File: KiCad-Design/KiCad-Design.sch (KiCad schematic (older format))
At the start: 66 parts, among them J1 USB_B_Micro, J2 Battery, J3 Ext, J4 OLED, Q1 SI2301, Q2 SI2301, Q3 SI2307CDS-T1-GE3, SW1 MCU BLE Adv, SW2 MCU FLASH, SW3 MCU RESET, U1 PMBT3904, U2 BME280, U3 CP2104, U4 LTC4054ES5-4.2, U5 PMBT3904, U6 PMBT3904, U7 BME680, U8 AP2112K-3.3, U9 ttgo-32-micro-symbols

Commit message: PCB : Small update on the PCB design
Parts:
- added R21, R22: 4.7K, Resistor_SMD:R_0805_2012Metric, symbol Device:R
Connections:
- net +3V3: now also R21.2, R22.2
- net MCU_SCL: now also R22.1
- net MCU_SDA: now also R21.1
- no-connect marks 36 -> 37
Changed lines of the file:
@@
 encoding utf-8
 Sheet 1 1
-Title ""
-Date ""
-Rev ""
-Comp ""
+Title "Google Home Environment Node"
+Date "2021-03-01"
+Rev "v1"
+Comp "RS System"
 Comment1 ""
 Comment2 ""
@@
 P 3000 5550
 F 0 "C6" V 3050 5450 50  0000 C CNN
-F 1 "100pF" V 3050 5700 50  0000 C CNN
+F 1 "100pF" V 3050 5700 50  0001 C CNN
 F 2 "Capacitor_SMD:C_0805_2012Metric" H 3038 5400 50  0001 C CNN
 F 3 "~" H 3000 5550 50  0001 C CNN
@@
 Wire Wire Line
 	5850 1900 5550 1900
-Text GLabel 5750 1300 2    50   BiDi Italic 0
+Text GLabel 5900 1300 2    50   BiDi Italic 0
 Sensor_add
-Wire Wire Line
-	5550 1300 5750 1300
-Text GLabel 5750 1700 2    50   BiDi Italic 0
+Text GLabel 5900 1700 2    50   BiDi Italic 0
 MCU_SDA
-Text GLabel 5750 1500 2    50   BiDi Italic 0
+Text GLabel 5900 1500 2    50   BiDi Italic 0
 MCU_SCL
-Wire Wire Line
-	5550 1500 5750 1500
-Wire Wire Line
-	5750 1700 5550 1700
 Wire Wire Line
 	4850 2200 4850 2300
@@
 	5200 5900 5150 5900
 Connection ~ 5150 5900
+NoConn ~ 5300 3950
+Wire Wire Line
+	5550 1300 5900 1300
+Wire Wire Line
+	5550 1500 5800 1500
+Wire Wire Line
+	5550 1700 5650 1700
+$Comp
+L Device:R R21
+U 1 1 60581768
+P 5650 1050
+F 0 "R21" V 5700 900 50  0000 C CNN
+F 1 "4.7K" V 5750 1050 50  0000 C CNN
+F 2 "Resistor_SMD:R_0805_2012Metric" V 5580 1050 50  0001 C CNN
+F 3 "~" H 5650 1050 50  0001 C CNN
+	1    5650 1050
+	-1   0    0    1
+$EndComp
+$Comp
+L Device:R R22
+U 1 1 605821B2
+P 5800 1050
+F 0 "R22" V 5850 900 50  0000 C CNN
+F 1 "4.7K" V 5700 1050 50  0000 C CNN
+F 2 "Resistor_SMD:R_0805_2012Metric" V 5730 1050 50  0001 C CNN
+F 3 "~" H 5800 1050 50  0001 C CNN
+	1    5800 1050
+	-1   0    0    1
+$EndComp
+$Comp
+L power:+3.3V #PWR051
+U 1 1 60582A40
+P 5900 650
+F 0 "#PWR051" H 5900 500 50  0001 C CNN
+F 1 "+3.3V" V 5915 778 50  0000 L CNN
+F 2 "" H 5900 650 50  0001 C CNN
+F 3 "" H 5900 650 50  0001 C CNN
+	1    5900 650
+	0    1    1    0
+$EndComp
+Wire Wire Line
+	5800 1200 5800 1500
+Connection ~ 5800 1500
+Wire Wire Line
+	5800 1500 5900 1500
+Wire Wire Line
+	5650 1200 5650 1700
+Connection ~ 5650 1700
+Wire Wire Line
+	5650 1700 5900 1700
+Wire Wire Line
+	5650 900  5650 650
+Wire Wire Line
+	5650 650  5800 650
+Wire Wire Line
+	5800 900  5800 650
+Connection ~ 5800 650
+Wire Wire Line
+	5800 650  5900 650
 $EndSCHEMATC

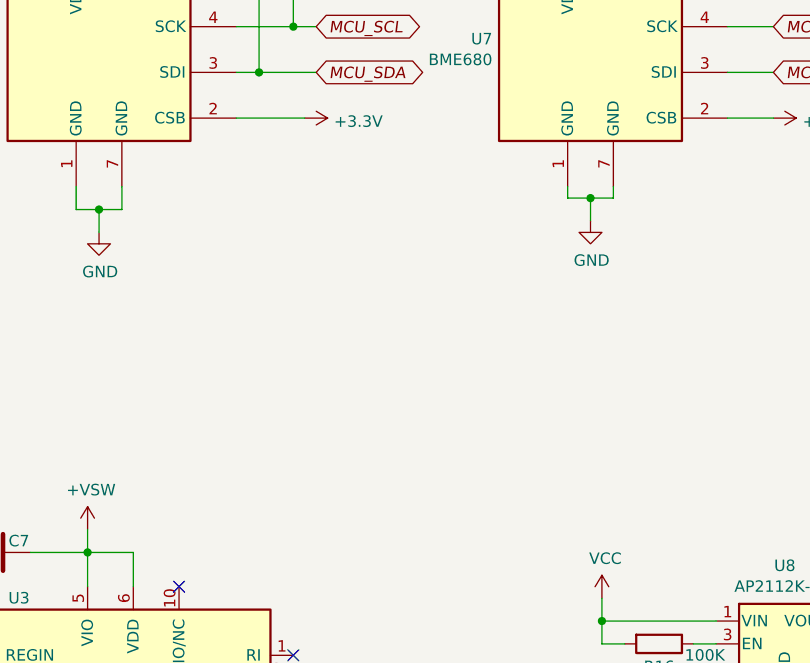
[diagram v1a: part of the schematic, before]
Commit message: PCB : Adding HDC1080 in the design
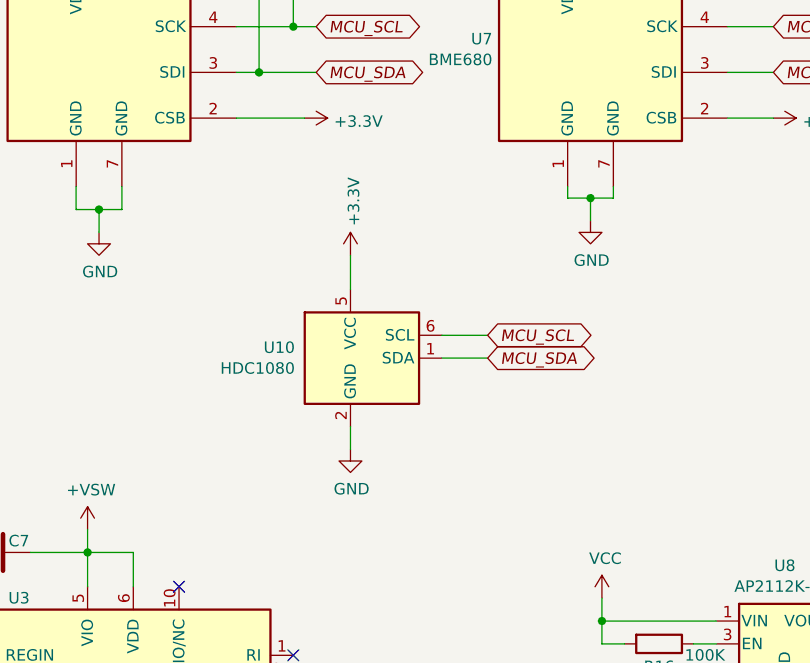
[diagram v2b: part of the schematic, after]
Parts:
- added U10: HDC1080, Package_SON:Texas_PWSON-N6, symbol Sensor_Humidity:HDC1080
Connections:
- net +3V3: now also U10.5 (VCC)
- net GND: now also U10.2 (GND)
- net MCU_SCL: now also U10.6 (SCL)
- net MCU_SDA: now also U10.1 (SDA)
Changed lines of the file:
@@
 Wire Wire Line
 	5800 650  5900 650
+$Comp
+L Sensor_Humidity:HDC1080 U10
+U 1 1 60508683
+P 6150 2950
+F 0 "U10" H 5807 2996 50  0000 R CNN
+F 1 "HDC1080" H 5807 2905 50  0000 R CNN
+F 2 "Package_SON:Texas_PWSON-N6" H 6100 2700 50  0001 L CNN
+F 3 "http://www.ti.com/lit/ds/symlink/hdc1080.pdf" H 5750 3200 50  0001 C CNN
+	1    6150 2950
+	1    0    0    -1
+$EndComp
+$Comp
+L power:+3.3V #PWR052
+U 1 1 60509223
+P 6050 2500
+F 0 "#PWR052" H 6050 2350 50  0001 C CNN
+F 1 "+3.3V" V 6065 2628 50  0000 L CNN
+F 2 "" H 6050 2500 50  0001 C CNN
+F 3 "" H 6050 2500 50  0001 C CNN
+	1    6050 2500
+	1    0    0    -1
+$EndComp
+$Comp
+L power:GND #PWR053
+U 1 1 605099FA
+P 6050 3350
+F 0 "#PWR053" H 6050 3100 50  0001 C CNN
+F 1 "GND" H 6055 3177 50  0000 C CNN
+F 2 "" H 6050 3350 50  0001 C CNN
+F 3 "" H 6050 3350 50  0001 C CNN
+	1    6050 3350
+	1    0    0    -1
+$EndComp
+Text GLabel 6650 2850 2    50   BiDi Italic 0
+MCU_SCL
+Text GLabel 6650 2950 2    50   BiDi Italic 0
+MCU_SDA
+Wire Wire Line
+	6050 2500 6050 2650
+Wire Wire Line
+	6450 2850 6650 2850
+Wire Wire Line
+	6650 2950 6450 2950
+Wire Wire Line
+	6050 3250 6050 3350
 $EndSCHEMATC

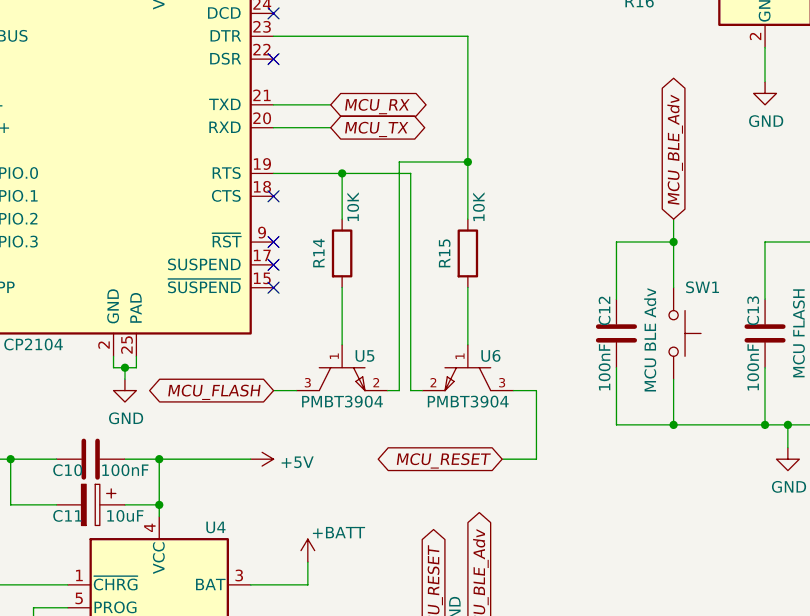
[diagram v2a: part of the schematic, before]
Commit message: PCB : Using UMH3N package instead of PMBT3904
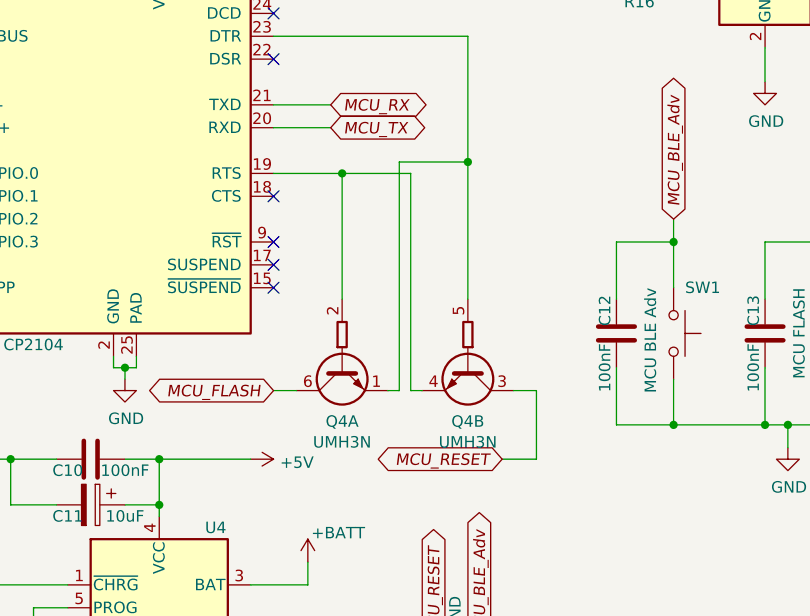
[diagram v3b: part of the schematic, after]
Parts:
- removed R14, R15: 10K, Resistor_SMD:R_0805_2012Metric, symbol Device:R
- removed U5, U6: PMBT3904, PMBT3904:NXP-PMBT3904,215-0, symbol PMBT3904:PMBT3904,215
- added Q4: UMH3N, Package_TO_SOT_SMD:SOT-363_SC-70-6, symbol Transistor_BJT:UMH3N
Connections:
- net MCU_FLASH: now also Q4.6 (C1)
- net MCU_RESET: now also Q4.3 (C2)
- net at U3.19 (RTS): now also Q4.2 (B1), Q4.4 (E2)
- net at U3.23 (DTR): now also Q4.1 (E1), Q4.5 (B2)
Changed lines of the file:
@@
 Wire Wire Line
 	5800 4850 6050 4850
-$Comp
-L Device:R R15
-U 1 1 60443C56
-P 6650 5400
-F 0 "R15" V 6550 5400 50  0000 C CNN
-F 1 "10K" V 6700 5600 50  0000 C CNN
-F 2 "Resistor_SMD:R_0805_2012Metric" V 6580 5400 50  0001 C CNN
-F 3 "~" H 6650 5400 50  0001 C CNN
-	1    6650 5400
-	1    0    0    -1
-$EndComp
-$Comp
-L Device:R R14
-U 1 1 60464BDE
-P 6100 5400
-F 0 "R14" V 6000 5400 50  0000 C CNN
-F 1 "10K" V 6150 5600 50  0000 C CNN
-F 2 "Resistor_SMD:R_0805_2012Metric" V 6030 5400 50  0001 C CNN
-F 3 "~" H 6100 5400 50  0001 C CNN
-	1    6100 5400
-	1    0    0    -1
-$EndComp
 Wire Wire Line
 	5800 5050 6100 5050
-Wire Wire Line
-	6100 5050 6100 5250
 Wire Wire Line
 	5800 4450 6650 4450
@@
 	6350 5000 6650 5000
 Connection ~ 6650 5000
-Wire Wire Line
-	6650 5000 6650 5250
 Text GLabel 5800 6000 0    50   BiDi Italic 0
 MCU_FLASH
@@
 	0    1    1    0
 $EndComp
-$Comp
-L PMBT3904:PMBT3904,215 U6
-U 1 1 604A948E
-P 6650 5700
-F 0 "U6" V 6800 5800 50  0000 C CNN
-F 1 "PMBT3904" V 7000 5700 50  0000 C CNN
-F 2 "PMBT3904:NXP-PMBT3904,215-0" H 6650 6200 50  0001 L CNN
-F 3 "https://assets.nexperia.com/documents/data-sheet/PMBT3904.pdf" H 6650 6300 50  0001 L CNN
-F 4 "IC" H 6650 6400 50  0001 L CNN "category"
-F 5 "1727-2959-1-ND" H 6650 6500 50  0001 L CNN "digikey description"
-F 6 "TRANS NPN 40V 0.2A SOT23" H 6650 6600 50  0001 L CNN "digikey part number"
-F 7 "yes" H 6650 6700 50  0001 L CNN "lead free"
-F 8 "8914a4d47db56a77" H 6650 6800 50  0001 L CNN "library id"
-F 9 "NXP" H 6650 6900 50  0001 L CNN "manufacturer"
-F 10 "771-PMBT3904-T/R" H 6650 7000 50  0001 L CNN "mouser part number"
-F 11 "SOT-23-3" H 6650 7100 50  0001 L CNN "package"
-F 12 "yes" H 6650 7200 50  0001 L CNN "rohs"
-F 13 "+150°C" H 6650 7300 50  0001 L CNN "temperature range high"
-F 14 "-65°C" H 6650 7400 50  0001 L CNN "temperature range low"
-	1    6650 5700
-	0    1    1    0
-$EndComp
-$Comp
-L PMBT3904:PMBT3904,215 U5
-U 1 1 604AA823
-P 6100 5700
-F 0 "U5" V 6250 5600 50  0000 C CNN
-F 1 "PMBT3904" V 6450 5700 50  0000 C CNN
-F 2 "PMBT3904:NXP-PMBT3904,215-0" H 6100 6200 50  0001 L CNN
-F 3 "https://assets.nexperia.com/documents/data-sheet/PMBT3904.pdf" H 6100 6300 50  0001 L CNN
-F 4 "IC" H 6100 6400 50  0001 L CNN "category"
-F 5 "1727-2959-1-ND" H 6100 6500 50  0001 L CNN "digikey description"
-F 6 "TRANS NPN 40V 0.2A SOT23" H 6100 6600 50  0001 L CNN "digikey part number"
-F 7 "yes" H 6100 6700 50  0001 L CNN "lead free"
-F 8 "8914a4d47db56a77" H 6100 6800 50  0001 L CNN "library id"
-F 9 "NXP" H 6100 6900 50  0001 L CNN "manufacturer"
-F 10 "771-PMBT3904-T/R" H 6100 7000 50  0001 L CNN "mouser part number"
-F 11 "SOT-23-3" H 6100 7100 50  0001 L CNN "package"
-F 12 "yes" H 6100 7200 50  0001 L CNN "rohs"
-F 13 "+150°C" H 6100 7300 50  0001 L CNN "temperature range high"
-F 14 "-65°C" H 6100 7400 50  0001 L CNN "temperature range low"
-	1    6100 5700
-	0    -1   1    0
-$EndComp
-Wire Wire Line
-	6650 5550 6650 5800
-Wire Wire Line
-	6100 5550 6100 5800
 Wire Wire Line
 	4900 3800 4650 3800
@@
 Wire Wire Line
 	6050 3250 6050 3350
+$Comp
+L Transistor_BJT:UMH3N Q4
+U 1 1 60511EC7
+P 6100 5800
+F 0 "Q4" V 6435 5800 50  0000 C CNN
+F 1 "UMH3N" V 6526 5800 50  0000 C CNN
+F 2 "Package_TO_SOT_SMD:SOT-363_SC-70-6" H 6105 5360 50  0001 C CNN
+F 3 "http://rohmfs.rohm.com/en/products/databook/datasheet/discrete/transistor/digital/emh3t2r-e.pdf" H 6250 5800 50  0001 C CNN
+	1    6100 5800
+	0    -1   1    0
+$EndComp
+$Comp
+L Transistor_BJT:UMH3N Q4
+U 2 1 6050FCBB
+P 6650 5800
+F 0 "Q4" V 6985 5800 50  0000 C CNN
+F 1 "UMH3N" V 7076 5800 50  0000 C CNN
+F 2 "Package_TO_SOT_SMD:SOT-363_SC-70-6" H 6655 5360 50  0001 C CNN
+F 3 "http://rohmfs.rohm.com/en/products/databook/datasheet/discrete/transistor/digital/emh3t2r-e.pdf" H 6800 5800 50  0001 C CNN
+	2    6650 5800
+	0    1    1    0
+$EndComp
+Wire Wire Line
+	6650 5000 6650 5600
+Wire Wire Line
+	6100 5050 6100 5600
 $EndSCHEMATC

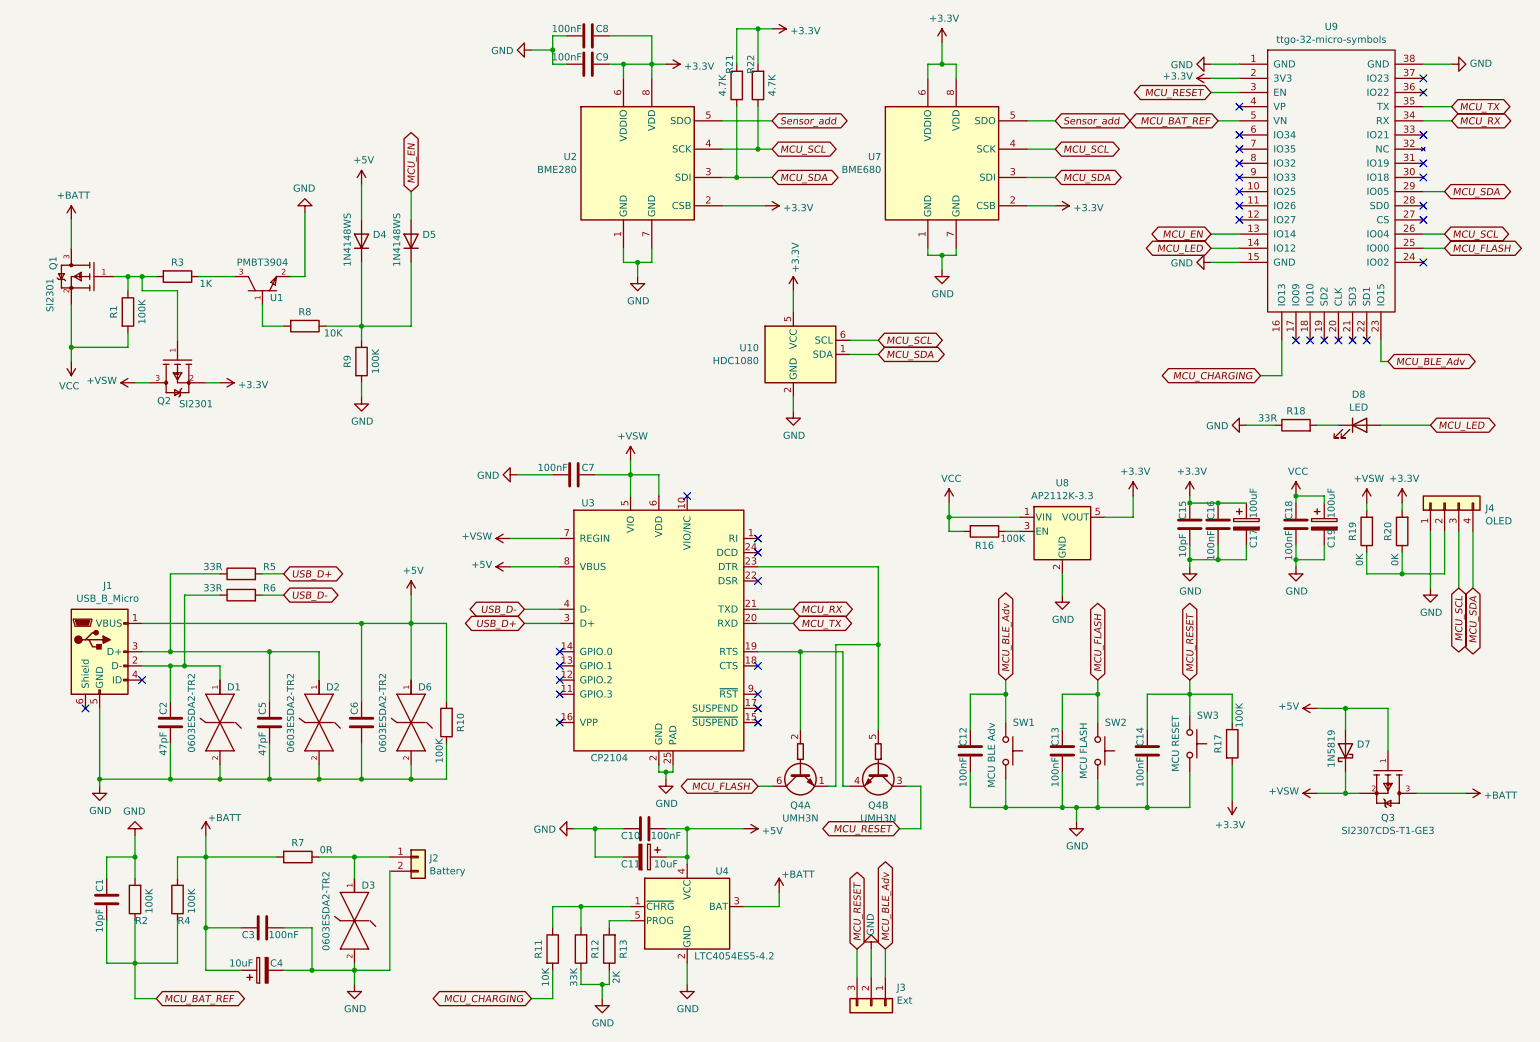
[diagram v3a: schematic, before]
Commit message: PCB : detaching the sensors from the main PCB
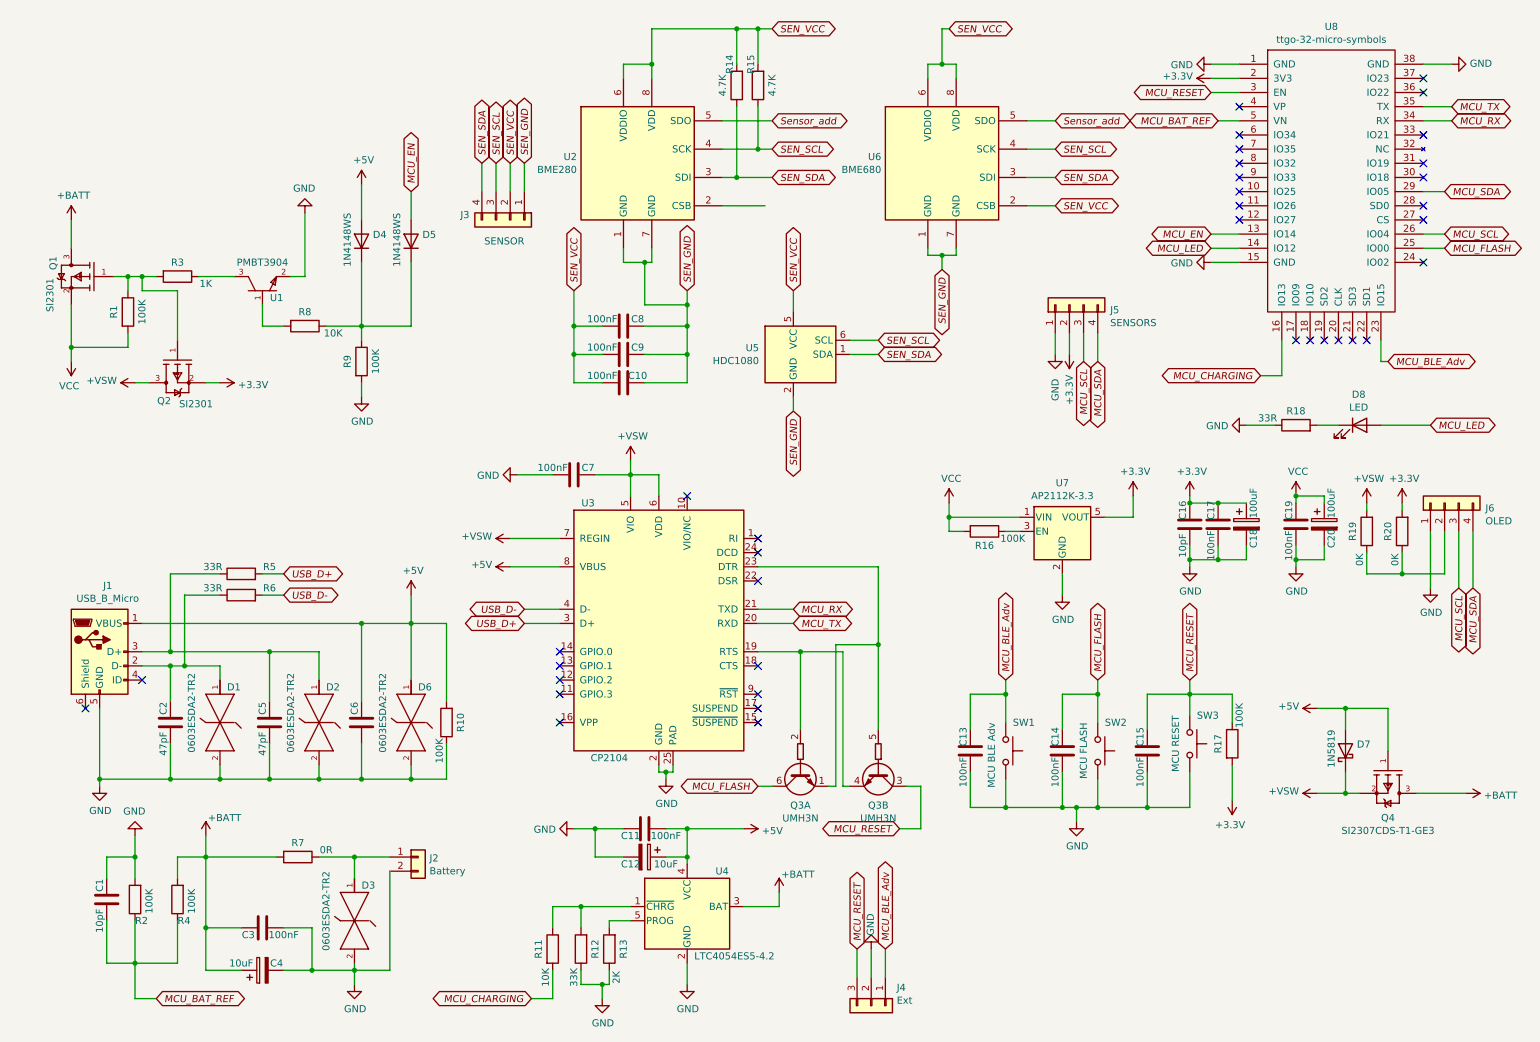
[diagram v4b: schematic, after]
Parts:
- added C9: 100nF, Capacitor_SMD:C_0805_2012Metric, symbol Device:C
- added J3: SENSOR, Connector_PinHeader_1.27mm:PinHeader_1x04_P1.27mm_Vertical, symbol Connector_Generic:Conn_01x04
- added J5: SENSORS, Connector_JST:JST_SH_BM04B-SRSS-TB_1x04-1MP_P1.00mm_Vertical, symbol Connector_Generic:Conn_01x04
- renumbered C8 to C10, C10 to C11, C11 to C12, C12 to C13, C13 to C14, C14 to C15, C15 to C16, C16 to C17, C17 to C18, C18 to C19, C19 to C20, C9 to C8, J3 to J4, J4 to J6, Q4 to Q3, Q3 to Q4, R21 to R14, R22 to R15, U10 to U5, U7 to U6, U8 to U7, U9 to U8
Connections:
- net +3V3: now also J5.2 (Pin_2); no longer C10.2, C8.2, R14.2, R15.2, U2.2 (CSB), U2.6 (VDDIO), U2.8 (VDD), U5.5 (VCC), U6.2 (CSB), U6.6 (VDDIO), U6.8 (VDD)
- net GND: now also J5.1 (Pin_1); no longer C10.1, C8.1, U2.1 (GND), U2.7 (GND), U5.2 (GND), U6.1 (GND), U6.7 (GND)
- net MCU_SCL: now also J5.3 (Pin_3); no longer R15.1, U2.4 (SCK), U5.6 (SCL), U6.4 (SCK)
- net MCU_SDA: now also J5.4 (Pin_4); no longer R14.1, U2.3 (SDI), U5.1 (SDA), U6.3 (SDI)
- new net SEN_GND: C10.2, C8.2, C9.2, J3.1 (Pin_1), U2.1 (GND), U2.7 (GND), U5.2 (GND), U6.1 (GND), U6.7 (GND)
- new net SEN_SCL: J3.3 (Pin_3), R15.1, U2.4 (SCK), U5.6 (SCL), U6.4 (SCK)
- new net SEN_SDA: J3.4 (Pin_4), R14.1, U2.3 (SDI), U5.1 (SDA), U6.3 (SDI)
- new net SEN_VCC: C10.1, C8.1, C9.1, J3.2 (Pin_2), R14.2, R15.2, U2.6 (VDDIO), U2.8 (VDD), U5.5 (VCC), U6.2 (CSB), U6.6 (VDDIO), U6.8 (VDD)
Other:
- moved on the sheet: C10, C8
